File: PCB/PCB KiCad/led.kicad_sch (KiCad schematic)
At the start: 22 parts, among them U5 TLC59208FIPWR

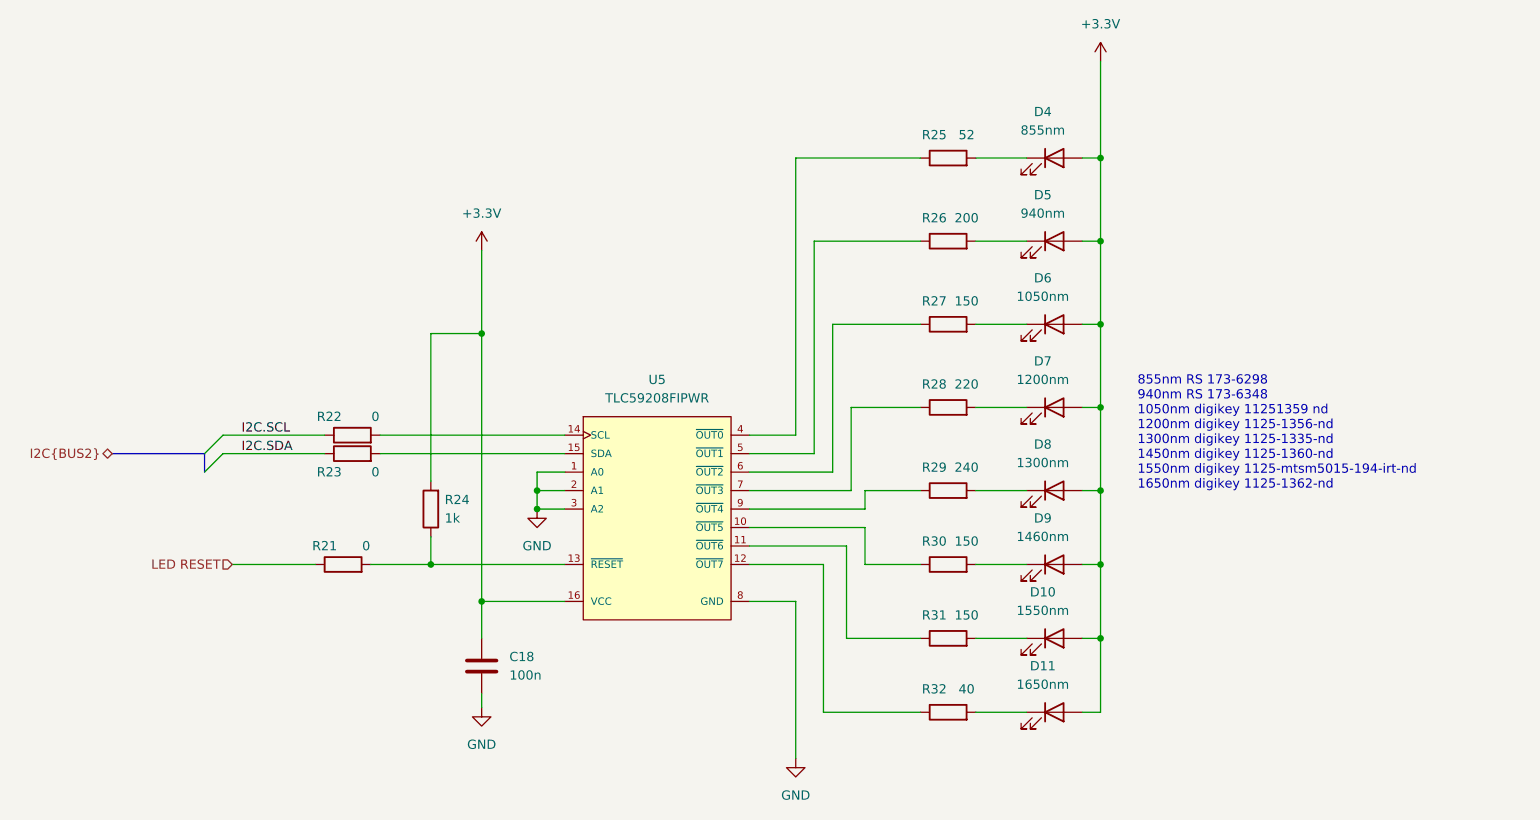
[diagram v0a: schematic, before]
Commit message: Updated IR emitter resistor values & alternative supply sources
The resistor values for the IR emitters in DB2.1 schematics were too high. Some of the emitters didn't even lit up.

I added new resistor values for the maximum forward current the emitters can handle. One option would be to balance the resistances for equal electrical output power of the emitters, but I haven't done research on what the actual optical output power would in that case be. In other words, if one would like the emitters lit the plastic sample with equal power. Please note, that the package of D4 and D5 is NOT 1206 and that they have a higher forward current than the other emitters.

The version number on the schematics is changed to 2.1.1. Please correct this, if it is wrong.

There are also alternative supply sources for the hard-to-get TI components and the 3.3V voltage regulator. These "clones" are tested and they seem to work, but I can't compare the signal quality to the original components since the stocks at official distributors are empty.
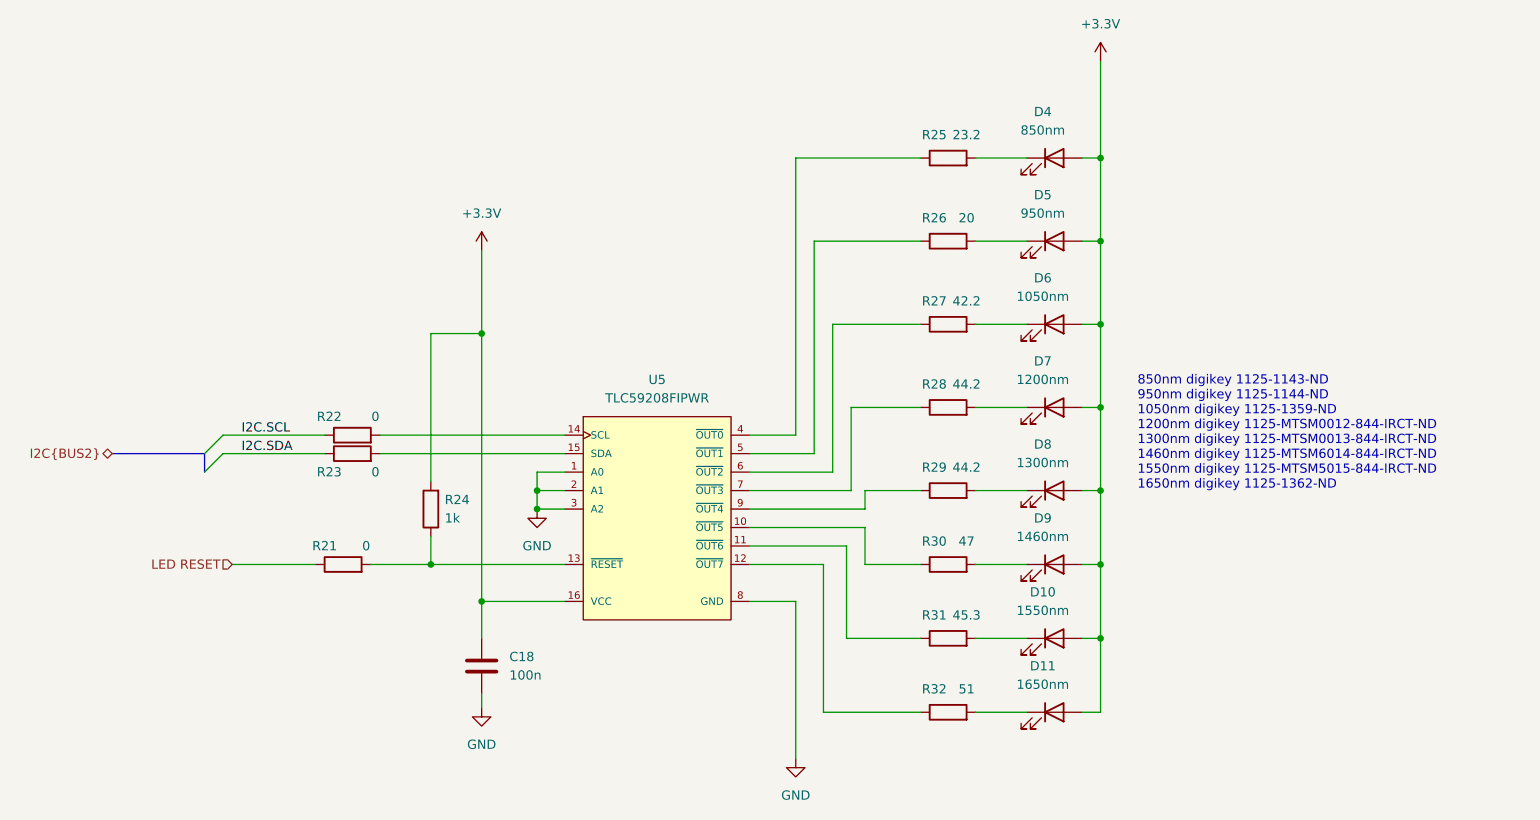
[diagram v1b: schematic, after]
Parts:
- D4: value 855nm -> 850nm
- D5: value 940nm -> 950nm
- R25: value 52 -> 23.2
- R26: value 200 -> 20
- R27: value 150 -> 42.2
- R28: value 220 -> 44.2
- R29: value 240 -> 44.2
- R30: value 150 -> 47
- R31: value 150 -> 45.3
- R32: value 40 -> 51
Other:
- note added: "850nm digikey 1125-1143-ND 950nm digikey 1125-1144-ND 1050nm digikey 1125-1359-ND 1200nm digikey 1125-MTSM0012-844-IRCT-ND 1300nm digikey 1125-MTSM0013-844-IRCT-ND 1460nm digikey 1125-MTSM6014-844-IRCT-ND 1550nm digikey 1125-MTSM5015-844-IRCT-ND 1650nm digikey 1125-1362-ND"
- note removed: "855nm RS 173-6298 940nm RS 173-6348 1050nm digikey 11251359 nd 1200nm digikey 1125-1356-nd 1300nm digikey 1125-1335-nd 1450nm digikey 1125-1360-nd 1550nm digikey 1125-mtsm5015-194-irt-nd 1650nm digikey 1125-1362-nd"
